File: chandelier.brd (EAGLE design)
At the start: 74 x 29.4 mm, 18 parts, among them IC1 NDC7002N-DUAL-MOS-N, IC2 NDC7002N-DUAL-MOS-N, IC3 NDC7002N-DUAL-MOS-N, IC4 NDC7002N-DUAL-MOS-N, IC9 74595, J1 HEADER, J10 HEADER, J2 HEADER, J3 HEADER, J4 HEADER, J5 HEADER, J6 HEADER, J7 HEADER, J8 HEADER, J9 HEADER

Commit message: adding uncommitted things
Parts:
- removed IC9: 74595, SparkFun-DigitalIC:TSSOP16
- removed U$1: RESISTOR-ARRAY-8, Livestream:CAY16-103J8
- added C1: 1uF, SparkFun-Capacitors:0805
- added IC5: 74595, SparkFun-DigitalIC:TSSOP16
- added IC6: RESISTOR-ARRAY-8, Livestream:CAY16-103J8
- added U$2, U$3: (no value), Livestream:HOLE-3
- moved J8 43.0 mm to (80.0, 14.9), turned to 330 degrees
- moved IC4 34.1 mm to (75.5, 10.4), turned to 270 degrees
- moved JP2 33.1 mm to (87.0, 1.00), turned to 90 degrees
- moved J7 24.4 mm to (70.0, 14.9), turned to 340 degrees
- moved J9 15.4 mm to (40.0, 4.90), turned to 90 degrees
- moved J5 15.3 mm to (50.0, 14.9), turned to 355 degrees
- moved J4 15.1 mm to (40.0, 14.9)
- moved J3 13.7 mm to (30.0, 14.9)
- moved IC2 12.1 mm to (34.2, 10.4), turned to 270 degrees
- moved J2 11.7 mm to (20.0, 14.9), turned to 20 degrees
- moved J1 9.52 mm to (10.0, 14.9), turned to 30 degrees
- moved JP1 9.08 mm to (3.00, 1.00), turned to 90 degrees
- moved J10 8.73 mm to (50.0, 4.90), turned to 270 degrees
- moved IC3 7.76 mm to (55.8, 10.4), turned to 270 degrees
- moved J6 7.29 mm to (60.0, 14.9), turned to 350 degrees
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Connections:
- removed net VCC: JP1.6, JP2.6
- net DIN: now also IC5.14; no longer IC9.14
- net DOUT: now also IC5.9; no longer IC9.9
- net G: now also IC5.13; no longer IC9.13
- net G1: now also IC5.15, IC6.2; no longer IC9.15, U$1.2
- net G2: now also IC5.1, IC6.4; no longer IC9.1, U$1.4
- net G3: now also IC5.2, IC6.6; no longer IC9.2, U$1.6
- net G4: now also IC5.3, IC6.8; no longer IC9.3, U$1.8
- net G5: now also IC5.4, IC6.10; no longer IC9.4, U$1.10
- net G6: now also IC5.5, IC6.12; no longer IC9.5, U$1.12
- net G7: now also IC5.6, IC6.14; no longer IC9.6, U$1.14
- net G8: now also IC5.7, IC6.16; no longer IC9.7, U$1.16
- net GND: now also C1.2, IC5.8, IC6.1, IC6.11, IC6.13, IC6.15, IC6.3, IC6.5, IC6.7, IC6.9; no longer IC9.8, U$1.1, U$1.11, U$1.13, U$1.15, U$1.3, U$1.5, U$1.7, U$1.9
- net RCK: now also IC5.12; no longer IC9.12
- net SCK: now also IC5.11; no longer IC9.11
- net VCC3V3: now also C1.1, IC5.10, IC5.16, JP1.6, JP2.6; no longer IC9.10, IC9.16
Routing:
- net GND: track 0.00 -> 147.0 mm, vias 0 -> 10
- net VCC3V3: track 0.00 -> 112.4 mm, vias 0 -> 1
- net DOUT: track 0.00 -> 75.6 mm, vias 0 -> 1
- net G: track 56.9 -> 129.9 mm, vias 0 -> 1
- net G8: track 0.00 -> 57.0 mm, vias 0 -> 3
- net G7: track 16.5 -> 68.0 mm
- net G6: track 0.00 -> 51.2 mm, vias 0 -> 3
- net G5: track 0.00 -> 47.5 mm, vias 0 -> 5
- net RCK: track 60.5 -> 97.9 mm, vias 2 -> 3
- net SCK: track 63.7 -> 98.5 mm, vias 2 -> 1
- net G1: track 0.00 -> 32.1 mm
- net G3: track 0.00 -> 27.7 mm
- net DIN: track 0.00 -> 23.3 mm, vias 0 -> 2
- net N$5: track 26.9 -> 6.39 mm
- net G2: track 0.00 -> 18.5 mm, vias 0 -> 2
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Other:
- board size 74 x 29.4 mm -> 90 x 21 mm

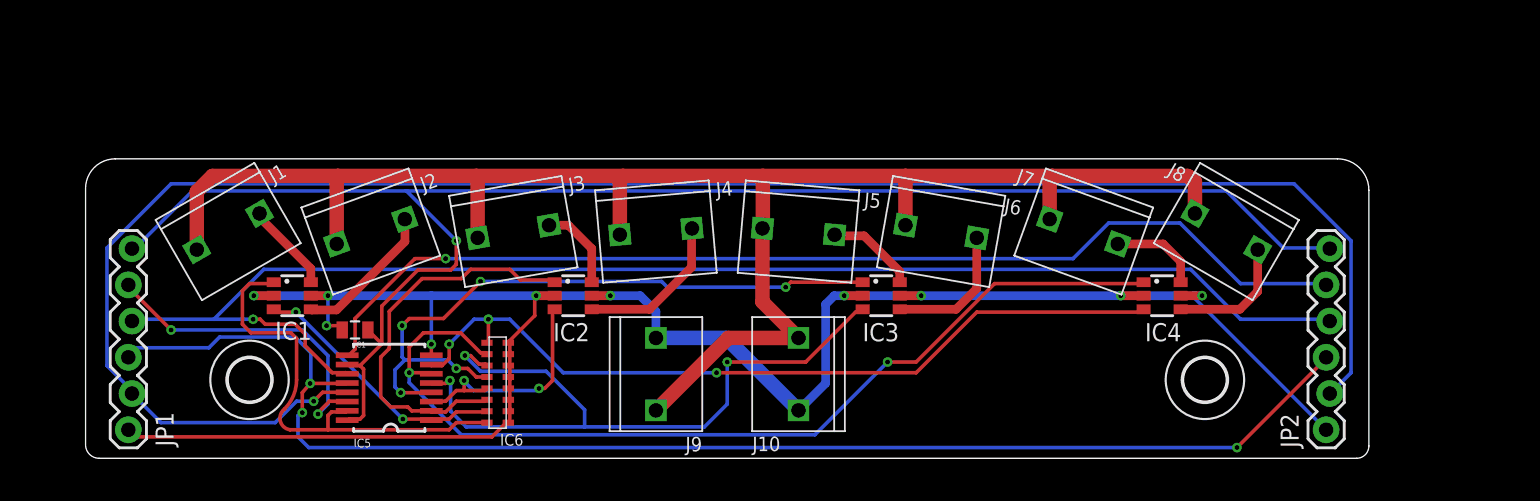
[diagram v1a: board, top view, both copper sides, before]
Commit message: added bom
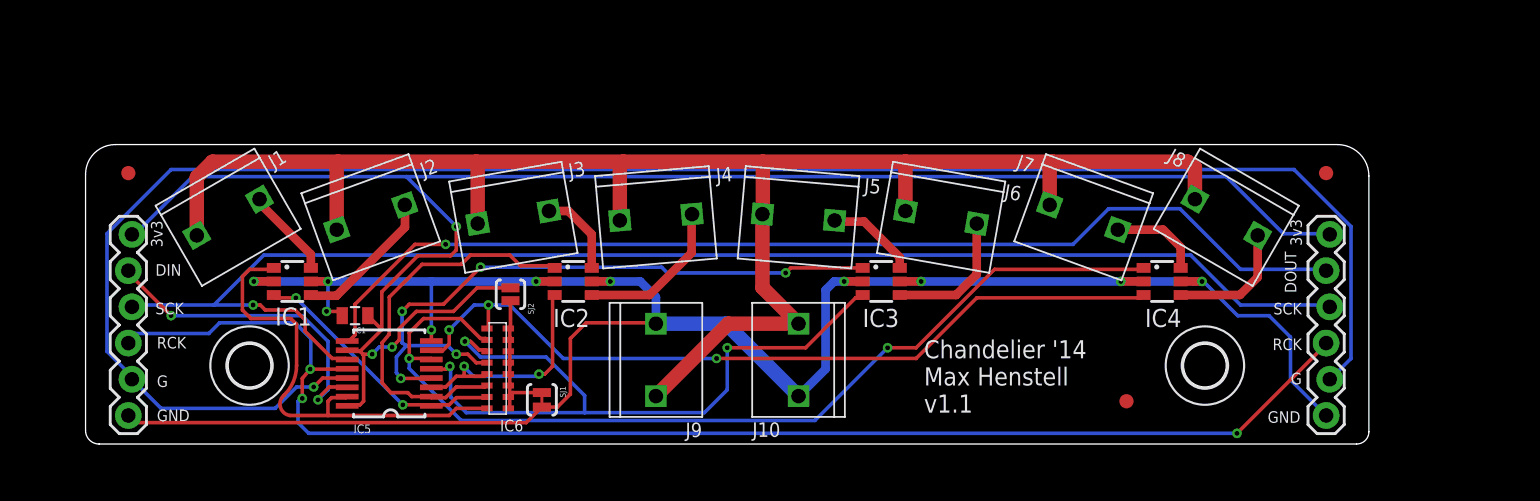
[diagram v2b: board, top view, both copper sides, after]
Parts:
- added SJ1: PULL DOWN, SparkFun-Passives:SJ_2S-TRACE
- added SJ2: PULL UP, SparkFun-Passives:SJ_2S-NO
- added U$1, U$4, U$5: FIDUCIAL, adafruit:FIDUCIAL_1MM
- JP1: value (none) -> INPUT
- JP2: value (none) -> OUTPUT
- moved IC5 1.00 mm to (21.4, 4.90)
- moved C1 1.00 mm to (18.9, 9.00)
- moved IC1 1.00 mm to (14.5, 11.4)
- moved IC2 1.00 mm to (34.2, 11.4)
- moved IC3 1.00 mm to (55.8, 11.4)
- moved IC4 1.00 mm to (75.5, 11.4)
- moved IC6 1.00 mm to (28.9, 5.30)
- moved J1 1.00 mm to (10.0, 15.9)
- moved J10 1.00 mm to (50.0, 5.90)
- moved J2 1.00 mm to (20.0, 15.9)
- moved J3 1.00 mm to (30.0, 15.9)
- moved J4 1.00 mm to (40.0, 15.9)
- moved J5 1.00 mm to (50.0, 15.9)
- moved J6 1.00 mm to (60.0, 15.9)
- moved J7 1.00 mm to (70.0, 15.9)
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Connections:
- new net N$9: IC6.1, IC6.11, IC6.13, IC6.15, IC6.3, IC6.5, IC6.7, IC6.9, SJ1.1, SJ2.1
- net GND: now also SJ1.2; no longer IC6.1, IC6.11, IC6.13, IC6.15, IC6.3, IC6.5, IC6.7, IC6.9
- net VCC3V3: now also SJ2.2
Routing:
- net VCC3V3: track 112.4 -> 125.1 mm, vias 1 -> 3
- net N$9: track 0.00 -> 10.7 mm
- net GND: track 147.0 -> 153.2 mm
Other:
- board text added: "3v3"
- board text added: "Chandelier '14 Max Henstell v1.1"
- board text added: "DIN"
- board text added: "DOUT"
- board text added: "G"
- board text added: "GND"
- board text added: "RCK"
- board text added: "SCK"

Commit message: updated board to fix footprint issue
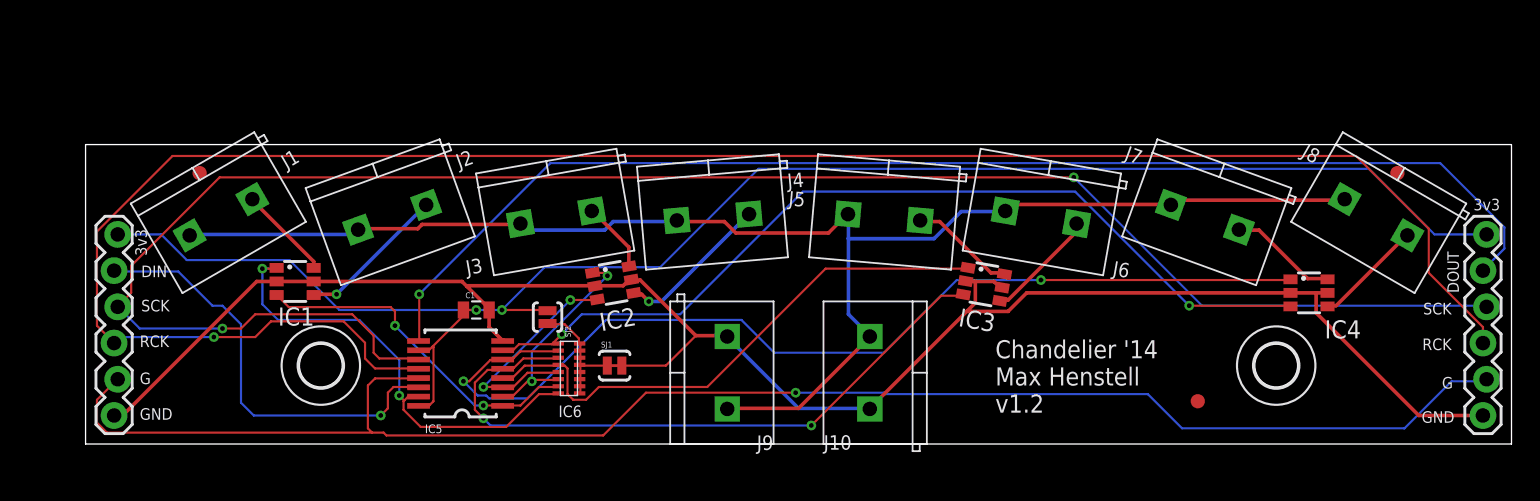
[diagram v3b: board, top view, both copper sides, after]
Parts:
- moved JP2 11.0 mm to (98.0, 2.00)
- moved J8 10.5 mm to (90.5, 15.9)
- moved IC4 10.3 mm to (85.8, 10.6)
- moved C1 8.51 mm to (27.4, 9.40), turned to 0 degrees
- moved J7 8.50 mm to (78.5, 15.9)
- moved IC3 7.20 mm to (63.0, 11.2), turned to 260 degrees
- moved J6 7.00 mm to (67.0, 15.9)
- moved J5 6.00 mm to (56.0, 15.9)
- moved SJ1 5.64 mm to (37.1, 5.50), turned to 0 degrees
- moved J10 5.08 mm to (55.0, 5.00)
- moved J9 5.08 mm to (45.0, 5.00)
- moved IC5 5.00 mm to (26.4, 4.90)
- moved IC6 5.00 mm to (33.9, 5.30)
- moved U$1 5.00 mm to (8.00, 19.0)
- moved U$2 5.00 mm to (83.5, 5.50)
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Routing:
- net RCK: track 97.9 -> 139.6 mm, vias 3 -> 1
- net SCK: track 98.5 -> 128.8 mm, vias 1 -> 2
- net GND: track 153.2 -> 128.8 mm, vias 10 -> 0
- net G: track 129.9 -> 112.4 mm
- net VCC24V: track 121.4 -> 105.3 mm
- net DOUT: track 75.6 -> 88.7 mm
- net G3: track 27.6 -> 15.2 mm, vias 0 -> 2
- net G5: track 47.4 -> 38.9 mm, vias 5 -> 0
- net VCC3V3: track 125.1 -> 118.0 mm, vias 3 -> 2
- net DIN: track 23.3 -> 30.3 mm, vias 2 -> 1
- net G8: track 57.0 -> 63.7 mm, vias 3 -> 2
- net G2: track 18.5 -> 24.2 mm
- net G6: track 51.2 -> 47.0 mm, vias 3 -> 2
- net G7: track 68.0 -> 71.4 mm
- net N$9: track 10.7 -> 8.82 mm
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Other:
- board size 90 x 21 mm -> 100 x 21 mm
- board text added: "Chandelier '14 Max Henstell v1.2"
- board text removed: "Chandelier '14 Max Henstell v1.1"

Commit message: fixed trace issues for 1.3
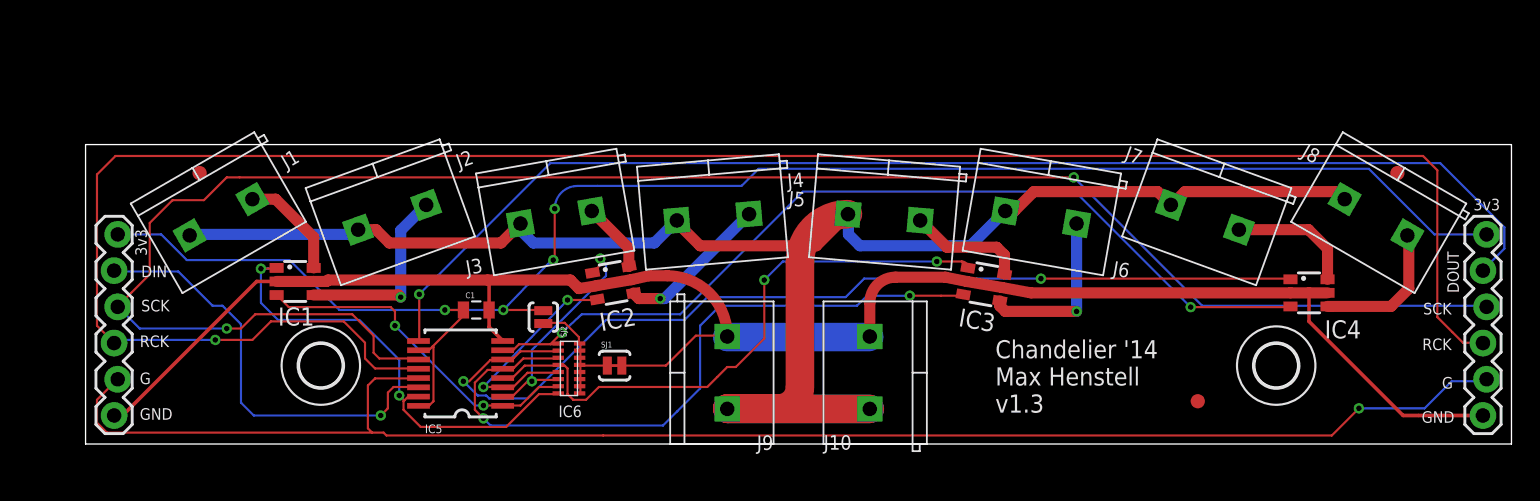
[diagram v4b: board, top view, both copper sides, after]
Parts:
- moved SJ2 0.30 mm to (32.1, 8.90)
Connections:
- net GND: now also J10.P1; no longer J10.P2
- net VCC24V: now also J10.P2; no longer J10.P1
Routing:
- net VCC24V: track 105.3 -> 131.0 mm
- net RCK: track 139.6 -> 145.5 mm
- net N$6: track 7.95 -> 12.1 mm, vias 0 -> 1
- net GND: track 128.8 -> 124.8 mm
- net N$2: track 10.5 -> 13.4 mm
- net G5: track 38.9 -> 41.7 mm, vias 0 -> 2
- net VCC3V3: track 118.0 -> 120.6 mm, vias 2 -> 4
- net G6: track 47.0 -> 49.6 mm
- net N$8: track 7.68 -> 9.99 mm
- net G: track 112.4 -> 110.4 mm
- net G7: track 71.4 -> 69.6 mm
- net G3: track 15.2 -> 16.7 mm
- net N$7: track 7.69 -> 8.91 mm
- net SCK: track 128.8 -> 129.8 mm
- net N$1: track 6.60 -> 7.56 mm
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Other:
- board text added: "Chandelier '14 Max Henstell v1.3"
- board text removed: "Chandelier '14 Max Henstell v1.2"
